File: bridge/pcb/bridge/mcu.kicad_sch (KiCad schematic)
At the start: 10 parts, among them J5 Conn_01x04, J6 Conn_01x02, J7 Conn_01x03, J8 Conn_01x02, J9 MCU_Test_Point, U1 L293, U3 AD557JN, U4 ATmega328P-P

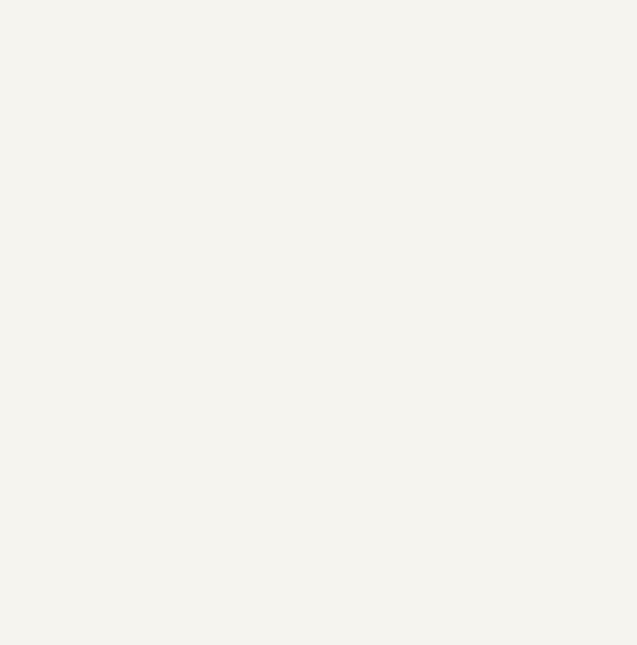
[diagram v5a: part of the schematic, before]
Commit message: Seperated 5V for accel pot and main 5V supply
Added 5V and 12V enable PCB headers
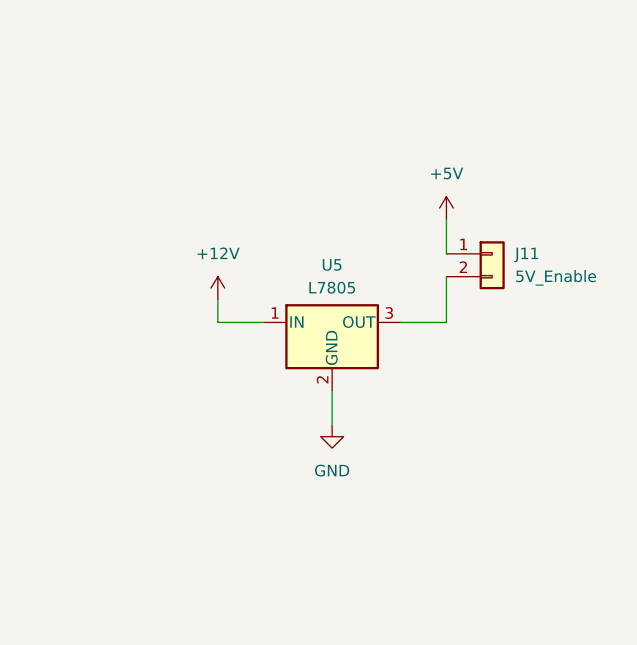
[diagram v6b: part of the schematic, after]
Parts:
- added J11: 5V_Enable, Connector_PinHeader_2.54mm:PinHeader_1x02_P2.54mm_Vertical, symbol Connector_Generic:Conn_01x02
- added U5: L7805, symbol Regulator_Linear:L7805
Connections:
- net +12V: now also U5.1 (IN)
- net +5V: now also J11.1 (Pin_1)
- net GND: now also U5.2 (GND)
- new net: J11.2 (Pin_2), U5.3 (OUT)
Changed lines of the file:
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@@
+    (stroke (width 0) (type default))
+  )
+  (wire (pts (xy 232.41 60.96) (xy 237.49 60.96))
     (stroke (width 0) (type default))
   )
@@
     (stroke (width 0) (type default))
   )
+  (wire (pts (xy 232.41 58.42) (xy 232.41 60.96))
+    (stroke (width 0) (type default))
+  )
   (wire (pts (xy 107.95 54.61) (xy 114.3 54.61))
     (stroke (width 0) (type default))
@@
     (stroke (width 0) (type default))
   )
+  (wire (pts (xy 245.11 68.58) (xy 245.11 72.39))
+    (stroke (width 0) (type default))
+  )
   (wire (pts (xy 99.06 171.45) (xy 101.6 171.45))
     (stroke (width 0) (type default))
   )
+  (wire (pts (xy 252.73 60.96) (xy 257.81 60.96))
+    (stroke (width 0) (type default))
+  )
   (wire (pts (xy 109.22 35.56) (xy 109.22 52.07))
     (stroke (width 0) (type default))
@@
     (stroke (width 0) (type default))
   )
+  (wire (pts (xy 257.81 49.53) (xy 257.81 53.34))
+    (stroke (width 0) (type default))
+  )
   (wire (pts (xy 48.26 25.4) (xy 48.26 24.13))
+    (stroke (width 0) (type default))
+  )
+  (wire (pts (xy 257.81 55.88) (xy 257.81 60.96))
     (stroke (width 0) (type default))
   )
@@
     )
   )
+  (symbol (lib_id "Connector_Generic:Conn_01x02") (at 262.89 53.34 0) (unit 1)
+    (in_bom yes) (on_board yes) (dnp no) (fields_autoplaced)
+    (property "Reference" "J11" (at 265.43 53.34 0)
+      (effects (font (size 1.27 1.27)) (justify left))
+    )
+    (property "Value" "5V_Enable" (at 265.43 55.88 0)
+      (effects (font (size 1.27 1.27)) (justify left))
+    )
+    (property "Footprint" "Connector_PinHeader_2.54mm:PinHeader_1x02_P2.54mm_Vertical" (at 262.89 53.34 0)
+      (effects (font (size 1.27 1.27)) hide)
+    )
+    (property "Datasheet" "~" (at 262.89 53.34 0)
+      (effects (font (size 1.27 1.27)) hide)
+    )
+    (pin "1")
+    (pin "2")
+    (instances
+      (project "bridge"
+        (path "/40a0f45e-7290-47b9-8da3-09f7dfbfbbd7/00f451ee-7b68-4840-8f31-2bfc247688fa"
+          (reference "J11") (unit 1)
+        )
+      )
+    )
+  )
   (symbol (lib_id "power:GND") (at 45.72 102.87 0) (unit 1)
     (in_bom yes) (on_board yes) (dnp no) (fields_autoplaced)
@@
     )
   )
+  (symbol (lib_id "power:GND") (at 245.11 72.39 0) (unit 1)
+    (in_bom yes) (on_board yes) (dnp no) (fields_autoplaced)
+    (property "Reference" "#PWR05" (at 245.11 78.74 0)
+      (effects (font (size 1.27 1.27)) hide)
+    )
+    (property "Value" "GND" (at 245.11 77.47 0)
+      (effects (font (size 1.27 1.27)))
+    )
+    (property "Footprint" "" (at 245.11 72.39 0)
+      (effects (font (size 1.27 1.27)) hide)
+    )
+    (property "Datasheet" "" (at 245.11 72.39 0)
+      (effects (font (size 1.27 1.27)) hide)
+    )
+    (pin "1")
+    (instances
+      (project "bridge"
+        (path "/40a0f45e-7290-47b9-8da3-09f7dfbfbbd7/00f451ee-7b68-4840-8f31-2bfc247688fa"
+          (reference "#PWR05") (unit 1)
+        )
+      )
+    )
+  )
   (symbol (lib_id "power:GND") (at 90.17 55.88 0) (unit 1)
     (in_bom yes) (on_board yes) (dnp no) (fields_autoplaced)
@@
         (path "/40a0f45e-7290-47b9-8da3-09f7dfbfbbd7/00f451ee-7b68-4840-8f31-2bfc247688fa"
           (reference "#PWR033") (unit 1)
+        )
+      )
+    )
+  )
+  (symbol (lib_id "power:+12V") (at 232.41 58.42 0) (unit 1)
+    (in_bom yes) (on_board yes) (dnp no) (fields_autoplaced)
+    (property "Reference" "#PWR035" (at 232.41 62.23 0)
+      (effects (font (size 1.27 1.27)) hide)
+    )
+    (property "Value" "+12V" (at 232.41 53.34 0)
+      (effects (font (size 1.27 1.27)))
+    )
+    (property "Footprint" "" (at 232.41 58.42 0)
+      (effects (font (size 1.27 1.27)) hide)
+    )
+    (property "Datasheet" "" (at 232.41 58.42 0)
+      (effects (font (size 1.27 1.27)) hide)
+    )
+    (pin "1")
+    (instances
+      (project "bridge"
+        (path "/40a0f45e-7290-47b9-8da3-09f7dfbfbbd7/00f451ee-7b68-4840-8f31-2bfc247688fa"
+          (reference "#PWR035") (unit 1)
         )
       )
@@
     )
   )
+  (symbol (lib_id "Regulator_Linear:L7805") (at 245.11 60.96 0) (unit 1)
+    (in_bom yes) (on_board yes) (dnp no) (fields_autoplaced)
+    (property "Reference" "U5" (at 245.11 54.61 0)
+      (effects (font (size 1.27 1.27)))
+    )
+    (property "Value" "L7805" (at 245.11 57.15 0)
+      (effects (font (size 1.27 1.27)))
+    )
+    (property "Footprint" "" (at 245.745 64.77 0)
+      (effects (font (size 1.27 1.27) italic) (justify left) hide)
+    )
+    (property "Datasheet" "http://www.st.com/content/ccc/resource/technical/document/datasheet/41/4f/b3/b0/12/d4/47/88/CD00000444.pdf/files/CD00000444.pdf/jcr:content/translations/en.CD00000444.pdf" (at 245.11 62.23 0)
+      (effects (font (size 1.27 1.27)) hide)
+    )
+    (pin "3")
+    (pin "2")
+    (pin "1")
+    (instances
+      (project "bridge"
+        (path "/40a0f45e-7290-47b9-8da3-09f7dfbfbbd7/00f451ee-7b68-4840-8f31-2bfc247688fa"
+          (reference "U5") (unit 1)
+        )
+      )
+    )
+  )
   (symbol (lib_id "power:GND") (at 101.6 173.99 0) (unit 1)
     (in_bom yes) (on_board yes) (dnp no) (fields_autoplaced)
@@
         )
       )
+    )
+  )
+  (symbol (lib_id "power:+5V") (at 257.81 49.53 0) (unit 1)
+    (in_bom yes) (on_board yes) (dnp no) (fields_autoplaced)
+    (property "Reference" "#PWR010" (at 257.81 53.34 0)
+      (effects (font (size 1.27 1.27)) hide)
+    )
+    (property "Value" "+5V" (at 257.81 44.45 0)
+      (effects (font (size 1.27 1.27)))
+    )
+    (property "Footprint" "" (at 257.81 49.53 0)
+      (effects (font (size 1.27 1.27)) hide)
+    )
+    (property "Datasheet" "" (at 257.81 49.53 0)
+      (effects (font (size 1.27 1.27)) hide)
+    )
+    (pin "1")
+    (instances
+      (project "bridge"
+        (path "/40a0f45e-7290-47b9-8da3-09f7dfbfbbd7/00f451ee-7b68-4840-8f31-2bfc247688fa"
+          (reference "#PWR010") (unit 1)
+        )
+      )

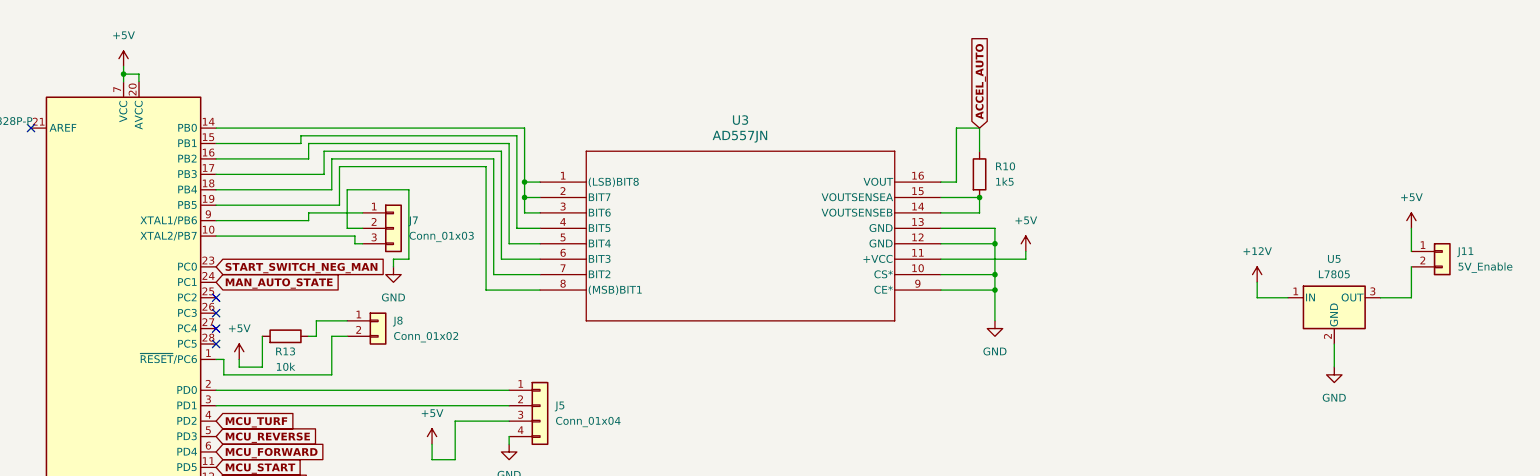
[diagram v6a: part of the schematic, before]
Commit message: Added capacitors near important components
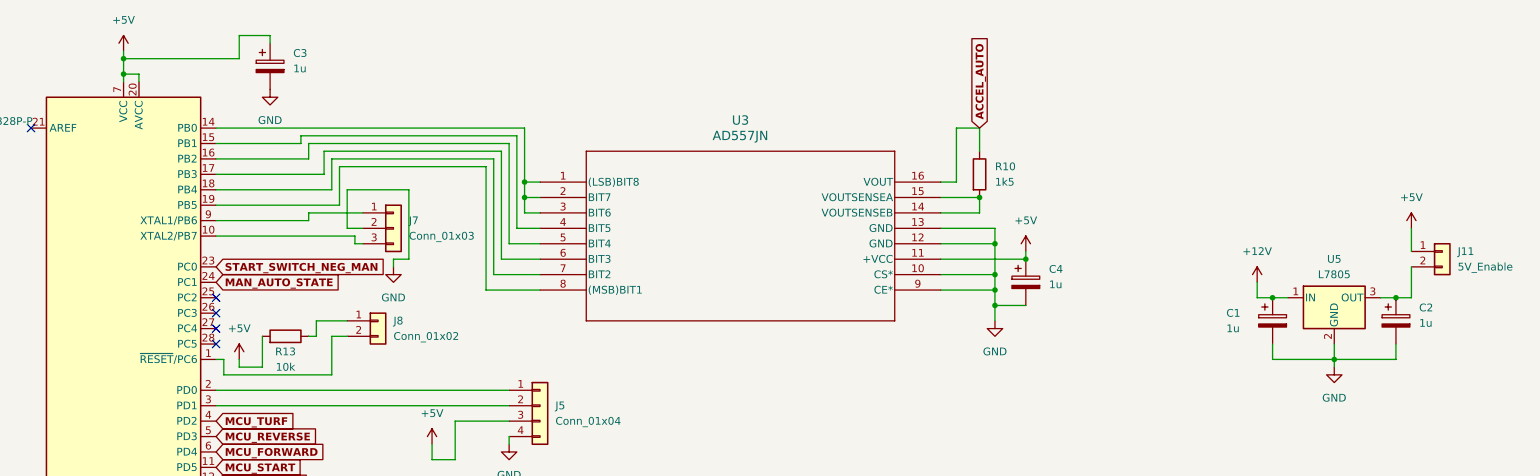
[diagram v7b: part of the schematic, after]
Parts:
- added C1, C2, C3, C4: 1u, symbol Device:C_Polarized
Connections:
- net +12V: now also C1.1
- net +5V: now also C3.1, C4.1
- net GND: now also C1.2, C2.2, C3.2, C4.2
- net at J11.2 (Pin_2), U5.3 (OUT): now also C2.1
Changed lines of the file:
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@@
   (junction (at 189.23 59.69) (diameter 0) (color 0 0 0 0)
   )
+  (junction (at 45.72 21.59) (diameter 0) (color 0 0 0 0)
+  )
+  (junction (at 255.27 60.96) (diameter 0) (color 0 0 0 0)
+  )
   (junction (at 189.23 52.07) (diameter 0) (color 0 0 0 0)
   )
+  (junction (at 189.23 62.23) (diameter 0) (color 0 0 0 0)
+  )
   (junction (at 189.23 57.15) (diameter 0) (color 0 0 0 0)
   )
+  (junction (at 194.31 54.61) (diameter 0) (color 0 0 0 0)
+  )
   (junction (at 99.06 171.45) (diameter 0) (color 0 0 0 0)
+  )
+  (junction (at 245.11 71.12) (diameter 0) (color 0 0 0 0)
+  )
+  (junction (at 234.95 60.96) (diameter 0) (color 0 0 0 0)
   )
   (no_connect (at 60.96 93.98))
@@
     (stroke (width 0) (type default))
   )
-  (wire (pts (xy 232.41 60.96) (xy 237.49 60.96))
+  (wire (pts (xy 232.41 60.96) (xy 234.95 60.96))
+    (stroke (width 0) (type default))
+  )
+  (wire (pts (xy 234.95 68.58) (xy 234.95 71.12))
     (stroke (width 0) (type default))
   )
@@
     (stroke (width 0) (type default))
   )
-  (wire (pts (xy 189.23 59.69) (xy 189.23 64.77))
+  (wire (pts (xy 245.11 71.12) (xy 245.11 72.39))
+    (stroke (width 0) (type default))
+  )
+  (wire (pts (xy 189.23 59.69) (xy 189.23 62.23))
     (stroke (width 0) (type default))
   )
@@
     (stroke (width 0) (type default))
   )
+  (wire (pts (xy 45.72 21.59) (xy 64.77 21.59))
+    (stroke (width 0) (type default))
+  )
   (wire (pts (xy 106.68 171.45) (xy 104.14 171.45))
     (stroke (width 0) (type default))
   )
+  (wire (pts (xy 234.95 71.12) (xy 245.11 71.12))
+    (stroke (width 0) (type default))
+  )
+  (wire (pts (xy 234.95 60.96) (xy 237.49 60.96))
+    (stroke (width 0) (type default))
+  )
   (wire (pts (xy 232.41 58.42) (xy 232.41 60.96))
     (stroke (width 0) (type default))
@@
     (stroke (width 0) (type default))
   )
+  (wire (pts (xy 64.77 21.59) (xy 64.77 17.78))
+    (stroke (width 0) (type default))
+  )
   (wire (pts (xy 39.37 123.19) (xy 39.37 127))
     (stroke (width 0) (type default))
@@
     (stroke (width 0) (type default))
   )
+  (wire (pts (xy 45.72 21.59) (xy 45.72 24.13))
+    (stroke (width 0) (type default))
+  )
   (wire (pts (xy 76.2 67.31) (xy 77.47 67.31))
     (stroke (width 0) (type default))
@@
     (stroke (width 0) (type default))
   )
+  (wire (pts (xy 255.27 68.58) (xy 255.27 71.12))
+    (stroke (width 0) (type default))
+  )
   (wire (pts (xy 92.71 54.61) (xy 90.17 54.61))
     (stroke (width 0) (type default))
@@
     (stroke (width 0) (type default))
   )
-  (wire (pts (xy 245.11 68.58) (xy 245.11 72.39))
+  (wire (pts (xy 245.11 68.58) (xy 245.11 71.12))
     (stroke (width 0) (type default))
   )
@@
     (stroke (width 0) (type default))
   )
-  (wire (pts (xy 252.73 60.96) (xy 257.81 60.96))
+  (wire (pts (xy 252.73 60.96) (xy 255.27 60.96))
     (stroke (width 0) (type default))
   )
@@
     (stroke (width 0) (type default))
   )
+  (wire (pts (xy 64.77 17.78) (xy 69.85 17.78))
+    (stroke (width 0) (type default))
+  )
   (wire (pts (xy 107.95 36.83) (xy 107.95 54.61))
     (stroke (width 0) (type default))
   )
+  (wire (pts (xy 189.23 62.23) (xy 189.23 64.77))
+    (stroke (width 0) (type default))
+  )
   (wire (pts (xy 78.74 36.83) (xy 107.95 36.83))
     (stroke (width 0) (type default))
@@
     (stroke (width 0) (type default))
   )
-  (wire (pts (xy 45.72 22.86) (xy 45.72 24.13))
+  (wire (pts (xy 45.72 20.32) (xy 45.72 21.59))
+    (stroke (width 0) (type default))
+  )
+  (wire (pts (xy 69.85 17.78) (xy 69.85 19.05))
     (stroke (width 0) (type default))
   )
@@
     (stroke (width 0) (type default))
   )
+  (wire (pts (xy 255.27 60.96) (xy 257.81 60.96))
+    (stroke (width 0) (type default))
+  )
   (wire (pts (xy 78.74 40.64) (xy 78.74 36.83))
     (stroke (width 0) (type default))
@@
     (stroke (width 0) (type default))
   )
+  (wire (pts (xy 189.23 62.23) (xy 194.31 62.23))
+    (stroke (width 0) (type default))
+  )
   (wire (pts (xy 111.76 44.45) (xy 111.76 41.91))
     (stroke (width 0) (type default))
@@
   )
   (wire (pts (xy 106.68 57.15) (xy 114.3 57.15))
+    (stroke (width 0) (type default))
+  )
+  (wire (pts (xy 255.27 71.12) (xy 245.11 71.12))
     (stroke (width 0) (type default))
   )
@@
     )
   )
-  (symbol (lib_id "power:+5V") (at 45.72 22.86 0) (unit 1)
-    (in_bom yes) (on_board yes) (dnp no) (fields_autoplaced)
-    (property "Reference" "#PWR031" (at 45.72 26.67 0)
-      (effects (font (size 1.27 1.27)) hide)
-    )
-    (property "Value" "+5V" (at 45.72 17.78 0)
-      (effects (font (size 1.27 1.27)))
-    )
-    (property "Footprint" "" (at 45.72 22.86 0)
-      (effects (font (size 1.27 1.27)) hide)
-    )
-    (property "Datasheet" "" (at 45.72 22.86 0)
+  (symbol (lib_id "Device:C_Polarized") (at 69.85 22.86 0) (unit 1)
+    (in_bom yes) (on_board yes) (dnp no) (fields_autoplaced)
+    (property "Reference" "C3" (at 73.66 20.701 0)
+      (effects (font (size 1.27 1.27)) (justify left))
+    )
+    (property "Value" "1u" (at 73.66 23.241 0)
+      (effects (font (size 1.27 1.27)) (justify left))
+    )
+    (property "Footprint" "" (at 70.8152 26.67 0)
+      (effects (font (size 1.27 1.27)) hide)
+    )
+    (property "Datasheet" "~" (at 69.85 22.86 0)
+      (effects (font (size 1.27 1.27)) hide)
+    )
+    (pin "2")
+    (pin "1")
+    (instances
+      (project "bridge"
+        (path "/40a0f45e-7290-47b9-8da3-09f7dfbfbbd7/00f451ee-7b68-4840-8f31-2bfc247688fa"
+          (reference "C3") (unit 1)
+        )
+      )
+    )
+  )
+  (symbol (lib_id "Device:C_Polarized") (at 194.31 58.42 0) (unit 1)
+    (in_bom yes) (on_board yes) (dnp no) (fields_autoplaced)
+    (property "Reference" "C4" (at 198.12 56.261 0)
+      (effects (font (size 1.27 1.27)) (justify left))
+    )
+    (property "Value" "1u" (at 198.12 58.801 0)
+      (effects (font (size 1.27 1.27)) (justify left))
+    )
+    (property "Footprint" "" (at 195.2752 62.23 0)
+      (effects (font (size 1.27 1.27)) hide)
+    )
+    (property "Datasheet" "~" (at 194.31 58.42 0)
+      (effects (font (size 1.27 1.27)) hide)
+    )
+    (pin "2")
+    (pin "1")
+    (instances
+      (project "bridge"
+        (path "/40a0f45e-7290-47b9-8da3-09f7dfbfbbd7/00f451ee-7b68-4840-8f31-2bfc247688fa"
+          (reference "C4") (unit 1)
+        )
+      )
+    )
+  )
+  (symbol (lib_id "power:+5V") (at 45.72 20.32 0) (unit 1)
+    (in_bom yes) (on_board yes) (dnp no) (fields_autoplaced)
+    (property "Reference" "#PWR031" (at 45.72 24.13 0)
+      (effects (font (size 1.27 1.27)) hide)
+    )
+    (property "Value" "+5V" (at 45.72 15.24 0)
+      (effects (font (size 1.27 1.27)))
+    )
+    (property "Footprint" "" (at 45.72 20.32 0)
+      (effects (font (size 1.27 1.27)) hide)
+    )
+    (property "Datasheet" "" (at 45.72 20.32 0)
       (effects (font (size 1.27 1.27)) hide)
     )
@@
     )
   )
+  (symbol (lib_id "power:GND") (at 69.85 26.67 0) (unit 1)
+    (in_bom yes) (on_board yes) (dnp no) (fields_autoplaced)
+    (property "Reference" "#PWR036" (at 69.85 33.02 0)
+      (effects (font (size 1.27 1.27)) hide)
+    )
+    (property "Value" "GND" (at 69.85 31.75 0)
+      (effects (font (size 1.27 1.27)))
+    )
+    (property "Footprint" "" (at 69.85 26.67 0)
+      (effects (font (size 1.27 1.27)) hide)
+    )
+    (property "Datasheet" "" (at 69.85 26.67 0)
+      (effects (font (size 1.27 1.27)) hide)
+    )
+    (pin "1")
+    (instances
+      (project "bridge"
+        (path "/40a0f45e-7290-47b9-8da3-09f7dfbfbbd7/00f451ee-7b68-4840-8f31-2bfc247688fa"
+          (reference "#PWR036") (unit 1)
+        )
+      )
+    )
+  )
   (symbol (lib_id "power:GND") (at 101.6 173.99 0) (unit 1)
     (in_bom yes) (on_board yes) (dnp no) (fields_autoplaced)
@@
         )
       )
+    )
+  )
+  (symbol (lib_id "Device:C_Polarized") (at 234.95 64.77 0) (unit 1)
+    (in_bom yes) (on_board yes) (dnp no)
+    (property "Reference" "C1" (at 227.33 63.5 0)
+      (effects (font (size 1.27 1.27)) (justify left))
+    )
+    (property "Value" "1u" (at 227.33 66.04 0)
+      (effects (font (size 1.27 1.27)) (justify left))
+    )
+    (property "Footprint" "" (at 235.9152 68.58 0)
+      (effects (font (size 1.27 1.27)) hide)
+    )
+    (property "Datasheet" "~" (at 234.95 64.77 0)
+      (effects (font (size 1.27 1.27)) hide)
+    )
+    (pin "2")
+    (pin "1")
+    (instances
+      (project "bridge"
+        (path "/40a0f45e-7290-47b9-8da3-09f7dfbfbbd7/00f451ee-7b68-4840-8f31-2bfc247688fa"
+          (reference "C1") (unit 1)
+        )
+      )
+    )
+  )
+  (symbol (lib_id "Device:C_Polarized") (at 255.27 64.77 0) (unit 1)
+    (in_bom yes) (on_board yes) (dnp no) (fields_autoplaced)
+    (property "Reference" "C2" (at 259.08 62.611 0)
+      (effects (font (size 1.27 1.27)) (justify left))
+    )
+    (property "Value" "1u" (at 259.08 65.151 0)
+      (effects (font (size 1.27 1.27)) (justify left))
+    )
+    (property "Footprint" "" (at 256.2352 68.58 0)
+      (effects (font (size 1.27 1.27)) hide)
+    )
+    (property "Datasheet" "~" (at 255.27 64.77 0)
+      (effects (font (size 1.27 1.27)) hide)
+    )
+    (pin "2")
+    (pin "1")
+    (instances
+      (project "bridge"
+        (path "/40a0f45e-7290-47b9-8da3-09f7dfbfbbd7/00f451ee-7b68-4840-8f31-2bfc247688fa"
+          (reference "C2") (unit 1)
+        )
+      )
